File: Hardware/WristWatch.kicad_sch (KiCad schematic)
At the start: 53 parts, among them J1 vcc, J2 gnd, J3 vcc, J4 gnd, Q1 Q_PMOS_GSD, U1 BQ51051BRHL, U3 LIS2DE12, U4 AP2205-3.0, U5 MCP73832-2-OT, U6 ESP32-C3, Y2 40M, Y3 32.768k

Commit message: Rev C hardware, gerbers, etc. Possible hardware bug flashing or with WiFi.
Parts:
- removed C10, C3, C6, C8: C_Small, Capacitor_SMD:C_0402_1005Metric, symbol Device:C_Small
- removed C11, C2: 470n, Capacitor_SMD:C_0402_1005Metric, symbol Device:C_Small
- removed C14, C15: 4u7, Capacitor_SMD:C_0402_1005Metric, symbol Device:C
- removed C5, C9: 10n, Capacitor_SMD:C_0402_1005Metric, symbol Device:C_Small
- removed J1, J3: vcc, TestPoint:TestPoint_Pad_D1.0mm, symbol Connector:Conn_01x01_Pin
- removed J2, J4: gnd, TestPoint:TestPoint_Pad_D1.0mm, symbol Connector:Conn_01x01_Pin
- removed L1: L, Connector_PinHeader_1.27mm:PinHeader_1x02_P1.27mm_Vertical, symbol Device:L
- removed R10: 10k, Resistor_SMD:R_0402_1005Metric, symbol Device:R
- removed R2, R3, R4, R5: R, Resistor_SMD:R_0402_1005Metric, symbol Device:R
- removed U1: BQ51051BRHL, Package_DFN_QFN:Texas_VQFN-RHL-20, symbol Battery_Management:BQ51051BRHL
- removed U5: MCP73832-2-OT, Package_TO_SOT_SMD:SOT-23-5, symbol Battery_Management:MCP73832-2-OT
- added R13: 100k, Resistor_SMD:R_0402_1005Metric, symbol Device:R_Small
- added R14: 124k, Resistor_SMD:R_0402_1005Metric, symbol Device:R_Small
- added TP4: BOOT, TestPoint:TestPoint_Pad_D1.5mm, symbol Connector:TestPoint
- added U5: VEML6030, VEML6030:VISHAY_VEML6030_2X2X0.87, symbol VEML6030:VEML6030
- C1: renamed from C12; value 1u -> 2.2u
- C10: renamed from C4; footprint (none) -> Capacitor_SMD:C_0402_1005Metric
- C11: renamed from C7; footprint (none) -> Capacitor_SMD:C_0402_1005Metric
- C12: renamed from C16; footprint (none) -> Capacitor_SMD:C_0402_1005Metric
- C2: renamed from C13; value 2u2 -> 2.2u
- C6: renamed from C17; footprint (none) -> Capacitor_SMD:C_0402_1005Metric
- C9: renamed from C1; footprint (none) -> Capacitor_SMD:C_0402_1005Metric
- TP3: value BOOT -> RST
- TP5: value VCC -> 3v3
- renumbered C20 to C3, C21 to C4, C22 to C5, C18 to C7, C19 to C8, L2 to L1, R9 to R1, R7 to R2, R8 to R3, R1 to R4, R12 to R5, U4 to U1, U3 to U2, U6 to U3, Y3 to Y1
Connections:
- net +BATT: now also R13.2
- net ESP_BOOT: now also TP4.1; no longer TP3.1
- net GND: now also U5.1, U5.4
- net SCL: now also U5.5
- net SDA: now also U5.2
- net RST: now reaches R5.1, U3.7 (CHIP_EN)
- net RST: now also TP3.1
- net ~{BAT_MEAS_EN}: now reaches U3.10 (MTDI)
- net ~{BAT_MEAS_EN}: now also R14.1
- net VEML_SUPPLY: now reaches U3.12 (MTCK)
- net VEML_SUPPLY: now also U5.6
- net IMU_SPAR_INT: no longer names the net of U2.11 (INT2)
- net IMU_SPAR_INT: no longer U3.9 (MTMS)
- new net BAT_MEAS_ADC: R13.1, R14.2, U3.9 (MTMS)
- no-connect marks 10 -> 9
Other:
- added sheet BMS (BMS.kicad_sch)
- moved on the sheet: AE1, C6, C7, C8, L1, Q1, R1, R4, R5, R6, U2, U3

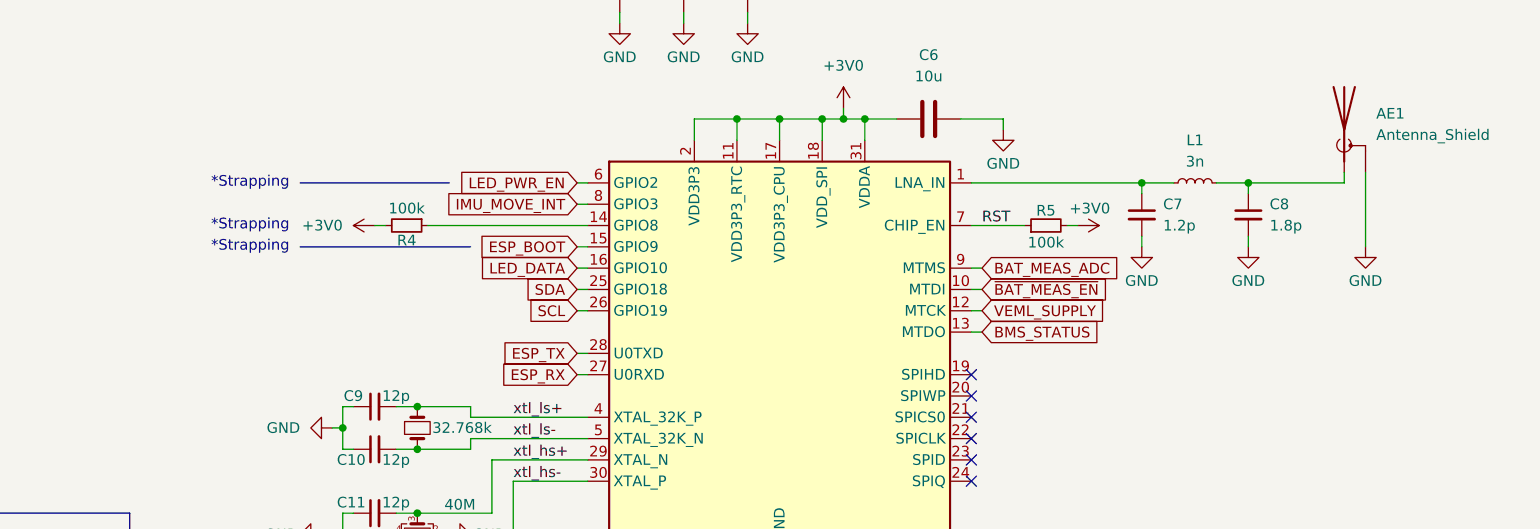
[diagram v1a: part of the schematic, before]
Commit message: add 100k external pull-up resistor to BMS Status line
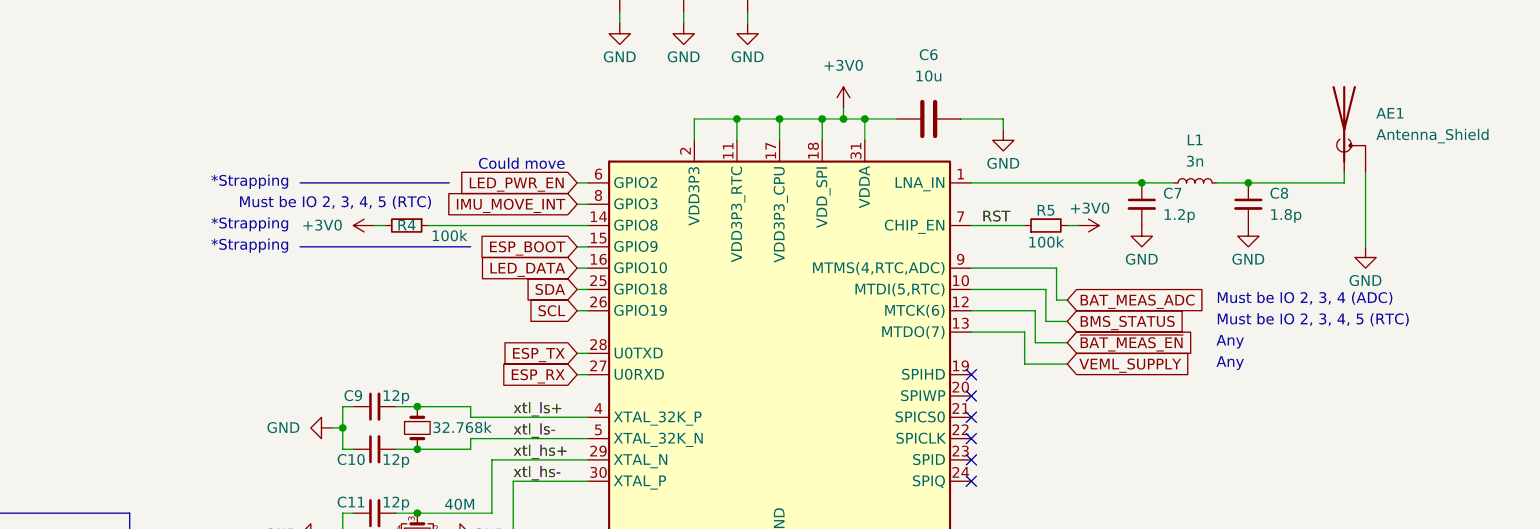
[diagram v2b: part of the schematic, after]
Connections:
- net BMS_STATUS: now also U3.10 (MTDI(5,RTC)); no longer U3.13 (MTDO)
- net VEML_SUPPLY: now also U3.13 (MTDO(7)); no longer U3.12 (MTCK)
- net ~{BAT_MEAS_EN}: now also U3.12 (MTCK(6)); no longer U3.10 (MTDI)
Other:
- note added: "Any"
- note added: "Could move"
- note added: "Must be IO 2, 3, 4 (ADC)"
- note added: "Must be IO 2, 3, 4, 5 (RTC)"
- moved on the sheet: C7, C8
